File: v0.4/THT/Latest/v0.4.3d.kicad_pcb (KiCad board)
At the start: 2 copper layers, 100 x 100 mm, 134 parts, among them IC3 Trig Cond Socket, J1 Conn_01x05, J2 Conn_01x06, J3 Conn_01x02, J4 Conn_02x20_Counter_Clockwise, J5 Conn_01x04, J6 Conn_01x05, J8 Conn_01x03, Q1 Q_NMOS_GDS, Q2 Q_NMOS_GDS, Q3 Q_NMOS_GDS, Q4 Q_NMOS_GDS, Q5 Q_NMOS_GDSD, Q6 Q_NMOS_GDSD, U1 SP721, U2 TC4424A, U3 SP721, U4 TC4424A, U5 MPX4250, U6 ULN2003, U8 LM2940S-5.0

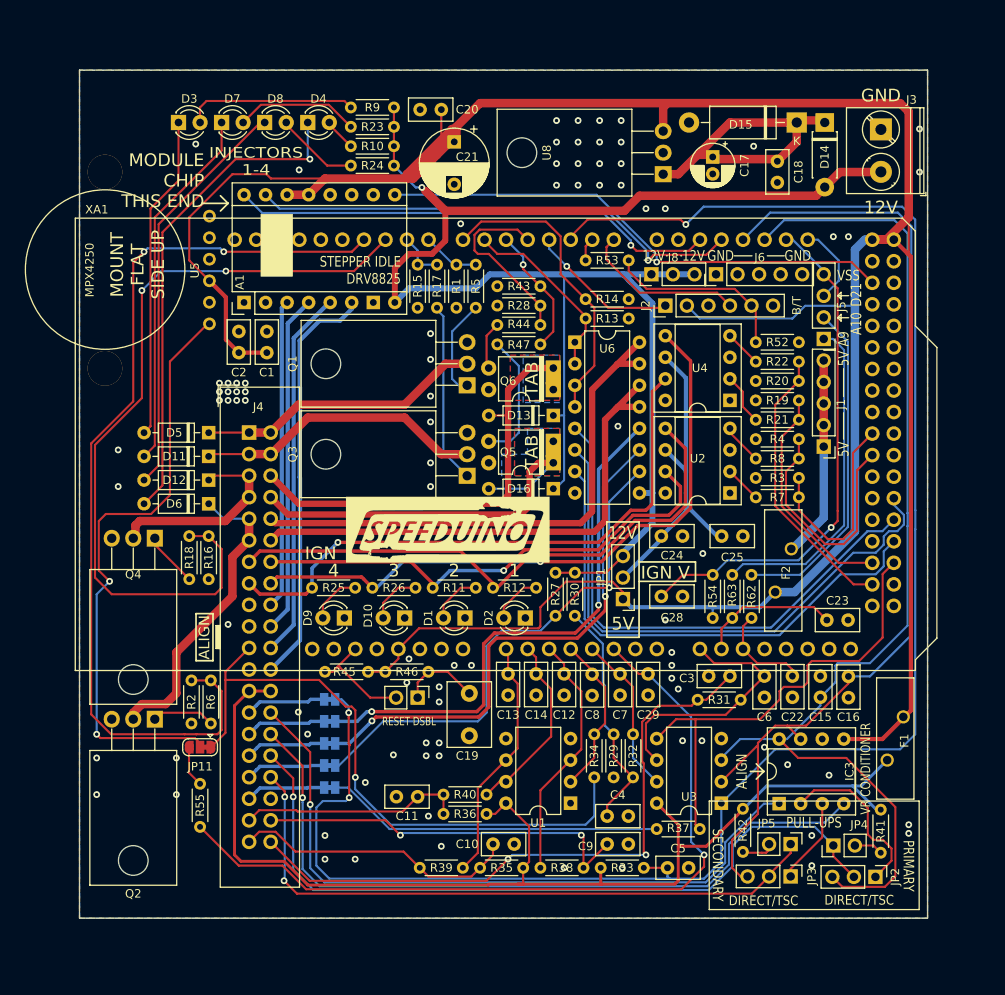
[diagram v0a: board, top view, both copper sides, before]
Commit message: Update v0.4.3d.kicad_pcb
fixed Q5 and Q6 to use TO-220 packages
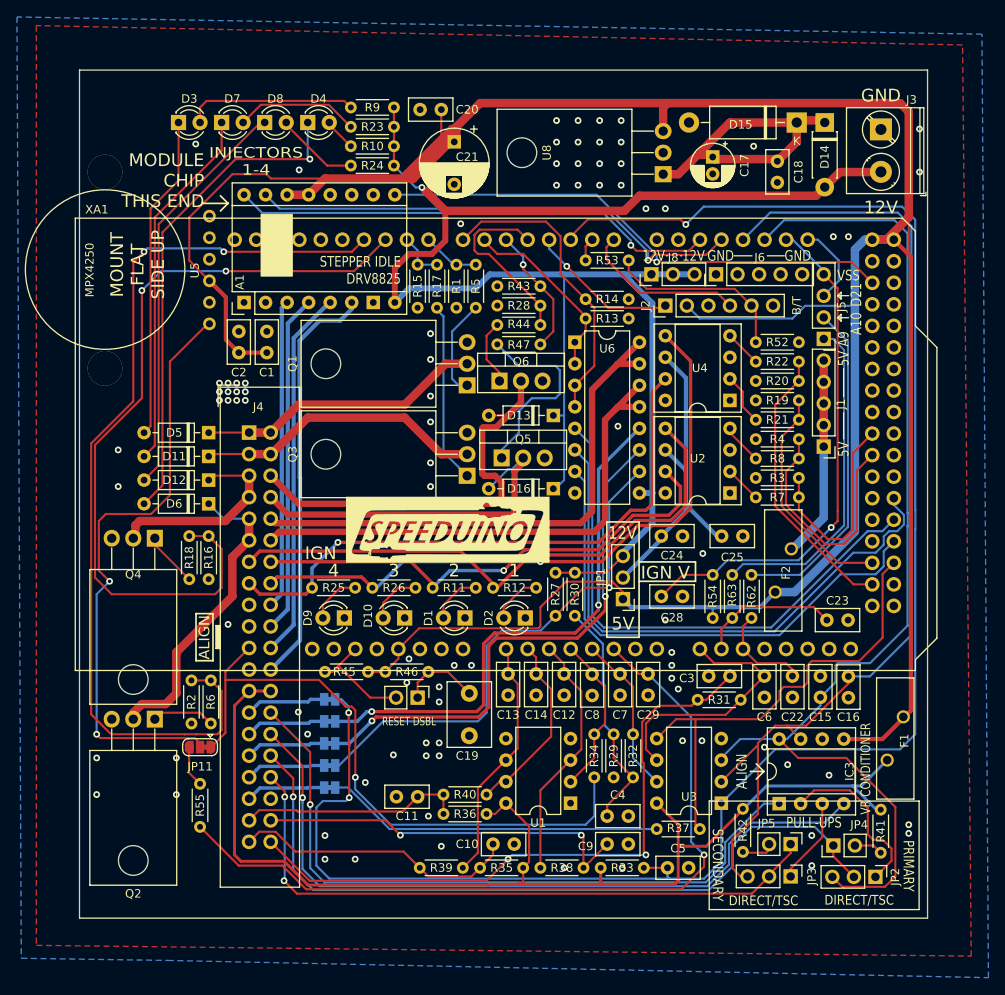
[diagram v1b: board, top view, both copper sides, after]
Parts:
- Q5, Q6: value Q_NMOS_GDSD -> TO-220-3_Vertical; footprint Package_DIP:Vishay_HVM-DIP-3_W7.62mm -> Package_TO_SOT_THT:TO-220-3_Vertical
- moved Q6 6.43 mm to (160.0, 73.7), turned to 0 degrees
- moved Q5 6.12 mm to (160.3, 82.7), turned to 0 degrees
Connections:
- Q5 pad 1: IDLE-OUT -> Net-(Q5-Pad2)
- Q5 pad 2: Net-(Q5-Pad2) -> IDLE-OUT
- Q6 pad 1: HC-2-OUT -> Net-(Q6-Pad2)
- Q6 pad 2: Net-(Q6-Pad2) -> HC-2-OUT
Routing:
- net IDLE-OUT: track 50.5 -> 42.3 mm
- net Net-(Q5-Pad2): track 15.4 -> 23.4 mm
- net HC-2-OUT: track 53.4 -> 49.4 mm
- net Net-(Q6-Pad2): track 5.71 -> 7.76 mm
- removed copper zone on B.Cu, net HC-2-OUT
- removed copper zone on F.Cu, net HC-2-OUT
- removed copper zone on B.Cu, net IDLE-OUT
- removed copper zone on F.Cu, net IDLE-OUT
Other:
- net class Default removed
- board text removed: "TAB"

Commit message: updated Q5 and Q6 to use TO-220 package
Q5 and Q6 used an outdated component that is no longer in production.

Updated components to use TO-220 packages which are more readily available.
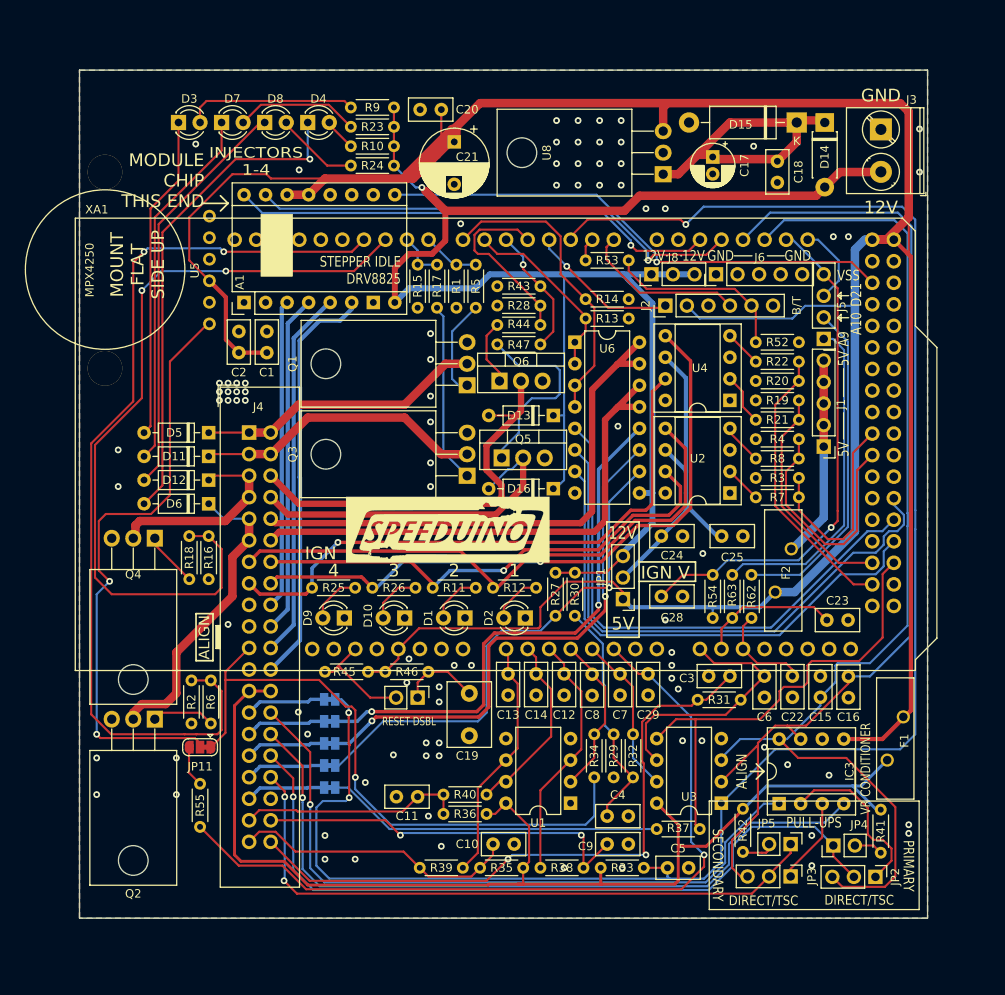
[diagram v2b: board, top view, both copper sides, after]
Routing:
- net IDLE-OUT: track 42.3 -> 41.0 mm
- net HC-2-OUT: track 49.4 -> 48.4 mm
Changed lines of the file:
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@@
   (segment (start 198.374 43.18) (end 198.12 42.926) (width 1) (layer "F.Cu") (net 26))
   (segment (start 198.12 42.926) (end 195.326 42.926) (width 1) (layer "F.Cu") (net 26))
-  (segment (start 162.814 82.733) (end 162.814 83.2955) (width 0.75) (layer "F.Cu") (net 27))
-  (segment (start 162.814 83.2955) (end 161.798 84.3115) (width 0.75) (layer "F.Cu") (net 27))
-  (segment (start 161.798 84.3115) (end 161.798 89.408) (width 0.75) (layer "F.Cu") (net 27))
+  (segment (start 162.814 86.179502) (end 159.585502 89.408) (width 0.75) (layer "F.Cu") (net 27))
+  (segment (start 159.585502 89.408) (end 135.088 89.408) (width 0.75) (layer "F.Cu") (net 27))
   (segment (start 135.088 89.408) (end 133.04 87.36) (width 0.75) (layer "F.Cu") (net 27))
-  (segment (start 161.798 89.408) (end 135.088 89.408) (width 0.75) (layer "F.Cu") (net 27))
+  (segment (start 162.814 82.733) (end 162.814 86.179502) (width 0.75) (layer "F.Cu") (net 27))
   (segment (start 158.75 86.36) (end 161.052 84.058) (width 0.25) (layer "B.Cu") (net 27))
   (segment (start 161.052 84.058) (end 161.489 84.058) (width 0.25) (layer "B.Cu") (net 27))
@@
   (segment (start 182.012 89.046) (end 182.012 88.032) (width 0.5) (layer "B.Cu") (net 79))
   (segment (start 174.582 96.838) (end 179.11 92.31) (width 0.5) (layer "B.Cu") (net 79))
-  (segment (start 159.512 84.836) (end 158.242 84.836) (width 0.75) (layer "F.Cu") (net 80))
-  (segment (start 159.512 88.138) (end 160.274 87.376) (width 0.75) (layer "F.Cu") (net 80))
-  (segment (start 161.036 77.724) (end 162.56 76.2) (width 0.75) (layer "F.Cu") (net 80))
-  (segment (start 158.75 77.724) (end 161.036 77.724) (width 0.25) (layer "F.Cu") (net 80))
-  (segment (start 157.988 84.582) (end 157.988 79.248) (width 0.75) (layer "F.Cu") (net 80))
-  (segment (start 160.274 85.598) (end 159.512 84.836) (width 0.75) (layer "F.Cu") (net 80))
-  (segment (start 162.56 76.2) (end 162.56 73.66) (width 0.75) (layer "F.Cu") (net 80))
-  (segment (start 160.274 87.376) (end 160.274 85.598) (width 0.75) (layer "F.Cu") (net 80))
-  (segment (start 133.04 84.82) (end 136.358 88.138) (width 0.75) (layer "F.Cu") (net 80))
-  (segment (start 136.358 88.138) (end 159.512 88.138) (width 0.75) (layer "F.Cu") (net 80))
-  (segment (start 157.988 79.248) (end 158.115 79.121) (width 0.75) (layer "F.Cu") (net 80))
-  (segment (start 158.242 84.836) (end 157.988 84.582) (width 0.75) (layer "F.Cu") (net 80))
-  (segment (start 158.115 79.121) (end 159.639 79.121) (width 0.75) (layer "F.Cu") (net 80))
-  (segment (start 159.639 79.121) (end 161.036 77.724) (width 0.75) (layer "F.Cu") (net 80))
+  (segment (start 162.56 77.216) (end 162.56 73.66) (width 0.75) (layer "F.Cu") (net 80))
+  (segment (start 158.496 81.28) (end 158.496 84.161456) (width 0.75) (layer "F.Cu") (net 80))
+  (segment (start 159.512 88.138) (end 136.358 88.138) (width 0.75) (layer "F.Cu") (net 80))
+  (segment (start 160.274 85.939456) (end 160.274 87.376) (width 0.75) (layer "F.Cu") (net 80))
+  (segment (start 158.75 77.724) (end 162.052 77.724) (width 0.25) (layer "F.Cu") (net 80))
+  (segment (start 158.496 84.161456) (end 160.274 85.939456) (width 0.75) (layer "F.Cu") (net 80))
+  (segment (start 162.052 77.724) (end 158.496 81.28) (width 0.75) (layer "F.Cu") (net 80))
+  (segment (start 160.274 87.376) (end 159.512 88.138) (width 0.75) (layer "F.Cu") (net 80))
+  (segment (start 162.052 77.724) (end 162.56 77.216) (width 0.75) (layer "F.Cu") (net 80))
+  (segment (start 136.358 88.138) (end 133.04 84.82) (width 0.75) (layer "F.Cu") (net 80))
   (segment (start 169.570001 90.424) (end 133.564 90.424) (width 0.75) (layer "F.Cu") (net 81))
   (segment (start 170.942 74.676) (end 170.942 89.052001) (width 0.75) (layer "F.Cu") (net 81))
@@
   (segment (start 160.02 72.644) (end 160.02 73.66) (width 0.25) (layer "F.Cu") (net 162))
   (zone (net 1) (net_name "GND") (layer "F.Cu") (hatch edge 0.5)
-    (connect_pads (clearance 0.25))
+    (connect_pads (clearance 0.5))
     (min_thickness 0.25) (filled_areas_thickness no)
     (fill yes (thermal_gap 0.5) (thermal_bridge_width 0.5))
     (polygon
       (pts
-        (xy 215.646 141.478)
-        (xy 214.63 34.036)
-        (xy 105.41 31.75)
-        (xy 105.41 140.208)
+        (xy 110.5 37)
+        (xy 210.5 37)
+        (xy 210.5 137)
+        (xy 110.5 137)
       )
     )
@@
   (zone (net 1) (net_name "GND") (layer "B.Cu") (hatch edge 0.5)
     (priority 1)
-    (connect_pads (clearance 0.25))
+    (connect_pads (clearance 0.5))
     (min_thickness 0.25) (filled_areas_thickness no)
     (fill yes (thermal_gap 0.5) (thermal_bridge_width 0.5))
     (polygon
       (pts
-        (xy 217.678 144.018)
-        (xy 216.916 32.766)
-        (xy 103.124 30.734)
-        (xy 103.632 141.732)
-        (xy 120.904 141.986)
+        (xy 110.5 37)
+        (xy 210.5 37)
+        (xy 210.5 137)
+        (xy 110.5 137)
       )
     )
